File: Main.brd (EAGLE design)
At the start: 125 x 30.3 mm, 41 parts, among them IC1 LM35CZ, Q1 IRLZ44N, T1 2N3904, U1 PIC18F45K22-I/P, X1 22-23-2021

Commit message: Schematic Rearranged
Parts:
- removed C11: (no value), resistor:153CLV-0505
- removed C12: (no value), resistor:C0805
- removed CR1, CR3: AMS1117, AMS1117:SOT223
- removed PSU2: PSU, con-wago-500:W237-102
- removed X1: 22-23-2021, con-molex:22-23-2021
- added C8: 100uF 10v, resistor:E2-5
- added C9: 100nF, resistor:C025-060X050
- added IC2: 7805TV, linear:TO220V
- added IC3: LD117AV33, v-reg:TO220L1
- added PSU1: PSU, con-wago-500:W237-102
- added R2: 0, resistor:0204/7
- C1: value (none) -> 100uF 10v; device resistor:153CLV-0505 -> resistor:E2-5
- C2: value (none) -> 100nF; device resistor:C0805 -> resistor:C025-060X050
- C3, C5: value (none) -> 330uF 16V; device resistor:153CLV-0505 -> resistor:E2-5
- C4, C6: device resistor:C0805 -> resistor:C025-024X044
- C7: value (none) -> 10uF 10v; device resistor:153CLV-0505 -> resistor:E2-5
- LED1, LED3: device led:SML0805 -> led:LED5MM
- R1, R3: value (none) -> 680Ω
- R10, R12, R13, R14, R4, R9: value 4k7 -> 4k7Ω
- R5: value 100 -> 100Ω
- R6, R7, R8: value 10k -> 10kΩ
- moved R12 1110.2 mm to (358.5, 354.1), turned to 90 degrees
- moved R5 1108.7 mm to (368.6, 336.2), turned to 90 degrees
- moved R10 1083.2 mm to (331.8, 347.2), turned to 90 degrees
- moved R9 1056.5 mm to (288.1, 345.4), turned to 90 degrees
- moved R4 1035.6 mm to (256.0, 345.2), turned to 90 degrees
- moved R3 1014.5 mm to (216.9, 345.6), turned to 90 degrees
- moved R1 994.8 mm to (179.9, 345.8), turned to 90 degrees
- moved R13 962.2 mm to (112.3, 348.7), turned to 90 degrees
- moved R14 957.3 mm to (152.1, 325.3), turned to 90 degrees
- moved R8 945.3 mm to (57.5, 349.5), turned to 90 degrees
- moved R7 913.4 mm to (-6.10, 332.3), turned to 90 degrees
- moved LED1 853.0 mm to (-1.27, -825.6), turned to 0 degrees
- moved R6 836.6 mm to (55.9, 266.1), turned to 90 degrees
- moved C2 821.2 mm to (-1.27, -799.5), flipped to the top, turned to 180 degrees
- moved C1 751.6 mm to (-118.9, -731.7), turned to 0 degrees
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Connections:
- net MCU_XI2 renamed MCU_MAIN_OSC2
- net MCU_XO2 renamed MCU_MAIN_OSC1
- net N$19 renamed DOUT_BUZZER
- net N$20 renamed AIN_LM35
- net N$7 renamed DIN_BUTTON_UP
- removed net N$17: R10.1, U$1.3, U1.18
- removed net N$18: R9.1, U$1.4, U1.23
- removed net N$5: R8.2, S4.3, S4.4, U1.36
- removed net N$8: R6.2, S2.3, S2.4, U1.38
- new net +12V: C3.+, C5.+, IC2.1, IC3.3, PSU.1, U$3.30
- new net DIN_BUTTON_DOWN: R8.2, S4.3, S4.4, U1.38
- new net DIN_LOCAL_REMOTE: R6.2, S2.3, S2.4, U1.36
- new net DOUT_HEATER: U1.17
- new net I2C_SCL: R10.2, U$1.3, U1.18
- new net I2C_SDA: R9.2, U$1.4, U1.23
- new net N$2: R2.1, U$3.1
- net +3V3: now also C8.+, C9.1, IC3.2, R2.2; no longer C11.+, C12.1, CR3.2, U$3.1
- net 12V: now also PSU1.1; no longer C3.+, C5.+, CR1.3, CR3.3, PSU.1, PSU2.1, X1.1
- net GND: now also C8.-, C9.2, IC2.2, IC3.1; no longer C11.-, C12.2, CR1.1, CR3.1, PSU2.2
- net N$1: now also LED3.K; no longer LED3.C
- net N$27: no longer U1.17
- net N$29: now also PSU1.2; no longer X1.2
- net N$3: now also LED1.K; no longer LED1.C
- net VCC: now also IC2.3, R10.1, R9.1; no longer CR1.2, R10.2, R9.2
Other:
- board size 125 x 30.3 mm -> 549.4 x 221.8 mm

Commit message: Renamed Resistors and capacitors
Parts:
- removed C1, C8: 100uF 10v, resistor:E2-5
- removed C2, C9: 100nF, resistor:C025-060X050
- removed C3: 330uF 16V, resistor:E2-5
- removed C4, C6: 22pF, resistor:C025-024X044
- removed C7: 10uF 10v, resistor:E2-5
- removed LED3: (no value), led:LED5MM
- removed PSU1: PSU, con-wago-500:W237-102
- removed R12, R4: 4k7Ω, resistor:0204/7
- removed R2: 0, resistor:0204/7
- removed R5: 100Ω, resistor:0204/7
- added C102, C105: 100uF 10v, resistor:E2-5
- added C103, C106: 100nF, resistor:C025-060X050
- added C104: 330uF 16V, resistor:E2-5
- added C107, C108: 22pF, resistor:C025-024X044
- added C109: 10uF 10v, resistor:E2-5
- added CN_HEATER: PSU, con-wago-500:W237-102
- added LED2: (no value), led:LED5MM
- added RX103, RX114: 4k7Ω, resistor:0204/7
- added RX104: 100Ω, resistor:0204/7
- added RX111: 0, resistor:0204/7
- IC2: value 7805TV -> 7805T; device linear:TO220V -> adafruit:TO220H
- moved IC2 949.1 mm to (47.0, 128.6)
- moved LED1 944.9 mm to (200.8, 97.5)
- moved SV1 670.6 mm to (60.4, 91.7)
- moved T1 391.4 mm to (15.7, 58.3), turned to 270 degrees
- moved SG1 369.9 mm to (15.7, 45.6), turned to 270 degrees
- moved IC1 330.7 mm to (15.7, 76.1), turned to 270 degrees
- moved Q3 292.2 mm to (42.1, 47.0), turned to 90 degrees
- moved U$1 130.3 mm to (100.4, 81.0)
- moved U$3 119.7 mm to (99.1, 42.3)
- moved Q1 116.8 mm to (6.81, 86.6), turned to 90 degrees
- moved S4 102.6 mm to (79.5, 89.2)
- moved S3 102.3 mm to (79.4, 80.0)
- moved S2 102.1 mm to (79.3, 70.9)
- moved IC3 90.9 mm to (62.0, 122.3)
- moved U1 80.3 mm to (60.0, 54.6)
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- renumbered C5 to C101, R1 to RX102, R10 to RX106, R13 to RX113, R14 to RX112, R3 to RX101, R6 to RX108, R7 to RX109, R8 to RX110, R9 to RX105
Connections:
- removed net 12V: PSU1.1
- removed net N$27: RX112.2, RX113.2
- net +12V: now also C104.+, CN_HEATER.1; no longer C3.+
- net +3V3: now also C105.+, C106.1, LED2.A, RX111.2; no longer C8.+, C9.1, LED3.A, R2.2
- net DOUT_BUZZER: now also RX114.2; no longer R12.2
- net DOUT_HEATER: now also RX112.2, RX113.2
- net GND: now also C102.-, C103.2, C104.-, C105.-, C106.2, C107.2, C108.2, C109.-; no longer C1.-, C2.2, C3.-, C4.2, C6.2, C7.-, C8.-, C9.2
- net MCLR: now also C109.+, RX103.1, RX104.2; no longer C7.+, R4.1, R5.2
- net MCU_MAIN_OSC1: now also C108.1; no longer C6.1
- net MCU_MAIN_OSC2: now also C107.1; no longer C4.1
- net N$1: now also LED2.K; no longer LED3.K
- net N$2: now also RX111.1; no longer R2.1
- net N$25: now also RX114.1; no longer R12.1
- net N$29: now also CN_HEATER.2; no longer PSU1.2
- net N$6: now also RX104.1; no longer R5.1
- net VCC: now also C102.+, C103.1, RX103.2; no longer C1.+, C2.1, R4.2

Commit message: Components placed, Previous to start routing
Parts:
- removed C101, C104: 330uF 16V, resistor:E2-5
- removed C102, C105: 100uF 10v, resistor:E2-5
- removed C103, C106: 100nF, resistor:C025-060X050
- removed C107, C108: 22pF, resistor:C025-024X044
- removed C109: 10uF 10v, resistor:E2-5
- removed RX101, RX102: 680Ω, resistor:0204/7
- removed RX103, RX105, RX106, RX112, RX113, RX114: 4k7Ω, resistor:0204/7
- removed RX104: 100Ω, resistor:0204/7
- removed RX108, RX109, RX110: 10kΩ, resistor:0204/7
- removed RX111: 0, resistor:0204/7
- added C1, C4: 330uF 16V, resistor:E2-5
- added C2, C5: 100uF 10v, resistor:E2-5
- added C3, C6: 100nF, resistor:C025-060X050
- added C7, C8: 22pF, resistor:C025-024X044
- added C9: 10uF 10v, resistor:E2-5
- added R1, R2: 680Ω, resistor:0204/7
- added R10, R8, R9: 10kΩ, resistor:0204/7
- added R11: 0, resistor:0204/7
- added R12, R13, R14, R3, R5, R6: 4k7Ω, resistor:0204/7
- added R4: 100Ω, resistor:0204/7
- IC1: value LM35CZ -> 7805T; device lm35:TO92 -> adafruit:TO220H
- IC2: value 7805T -> LD117AV33; device adafruit:TO220H -> v-reg:TO220L1
- IC3: value LD117AV33 -> LM35CZ; device v-reg:TO220L1 -> lm35:TO92
- moved LED1 174.7 mm to (27.8, 72.7), turned to 180 degrees
- moved LED2 153.1 mm to (48.1, 72.7), turned to 180 degrees
- moved IC3 102.8 mm to (5.31, 36.5), turned to 270 degrees
- moved S4 80.6 mm to (25.9, 29.0), turned to 180 degrees
- moved S3 80.1 mm to (26.0, 20.3), turned to 180 degrees
- moved SV1 61.7 mm to (4.04, 66.4), turned to 270 degrees
- moved S2 61.7 mm to (26.1, 39.6), turned to 180 degrees
- moved IC2 42.3 mm to (51.8, 86.6)
- moved S1 40.9 mm to (26.1, 51.1)
- moved Q3 38.6 mm to (26.6, 11.7), turned to 180 degrees
- moved T1 38.5 mm to (5.31, 21.2)
- moved PSU 38.1 mm to (9.88, 96.0)
- moved CN_HEATER 38.1 mm to (9.93, 81.3)
- moved SG1 35.1 mm to (10.0, 10.9), turned to 180 degrees
- moved Q1 34.9 mm to (4.27, 51.8)
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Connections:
- net +12V: now also C1.+, C4.+, IC1.1, IC2.3; no longer C101.+, C104.+, IC2.1, IC3.3
- net +3V3: now also C5.+, C6.1, IC2.2, R11.2; no longer C105.+, C106.1, IC3.2, RX111.2
- net AIN_LM35: now also IC3.2; no longer IC1.2
- net DIN_BUTTON_DOWN: now also R10.2; no longer RX110.2
- net DIN_BUTTON_UP: now also R9.2; no longer RX109.2
- net DIN_LOCAL_REMOTE: now also R8.2; no longer RX108.2
- net DOUT_BUZZER: now also R14.2; no longer RX114.2
- net DOUT_HEATER: now also R12.2, R13.2; no longer RX112.2, RX113.2
- net GND: now also C1.-, C2.-, C3.2, C4.-, C5.-, C6.2, C7.2, C8.2, C9.-, IC1.2, IC2.1, IC3.3, R1.1, R10.1, R13.1, R2.1, R8.1, R9.1; no longer C101.-, C102.-, C103.2, C104.-, C105.-, C106.2, C107.2, C108.2, C109.-, IC1.3, IC2.2, IC3.1, RX101.1, RX102.1, RX108.1, RX109.1, RX110.1, RX113.1
- net I2C_SCL: now also R6.2; no longer RX106.2
- net I2C_SDA: now also R5.2; no longer RX105.2
- net MCLR: now also C9.+, R3.1, R4.2; no longer C109.+, RX103.1, RX104.2
- net MCU_MAIN_OSC1: now also C8.1; no longer C108.1
- net MCU_MAIN_OSC2: now also C7.1; no longer C107.1
- net N$1: now also R2.2; no longer RX102.2
- net N$2: now also R11.1; no longer RX111.1
- net N$25: now also R14.1; no longer RX114.1
- net N$28: now also R12.1; no longer RX112.1
- net N$3: now also R1.2; no longer RX101.2
- net N$6: now also R4.1; no longer RX104.1
- net VCC: now also C2.+, C3.1, IC1.3, IC3.1, R3.2, R5.1, R6.1; no longer C102.+, C103.1, IC1.1, IC2.3, RX103.2, RX105.1, RX106.1
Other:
- board size 549.4 x 221.8 mm -> 91.2 x 105.5 mm

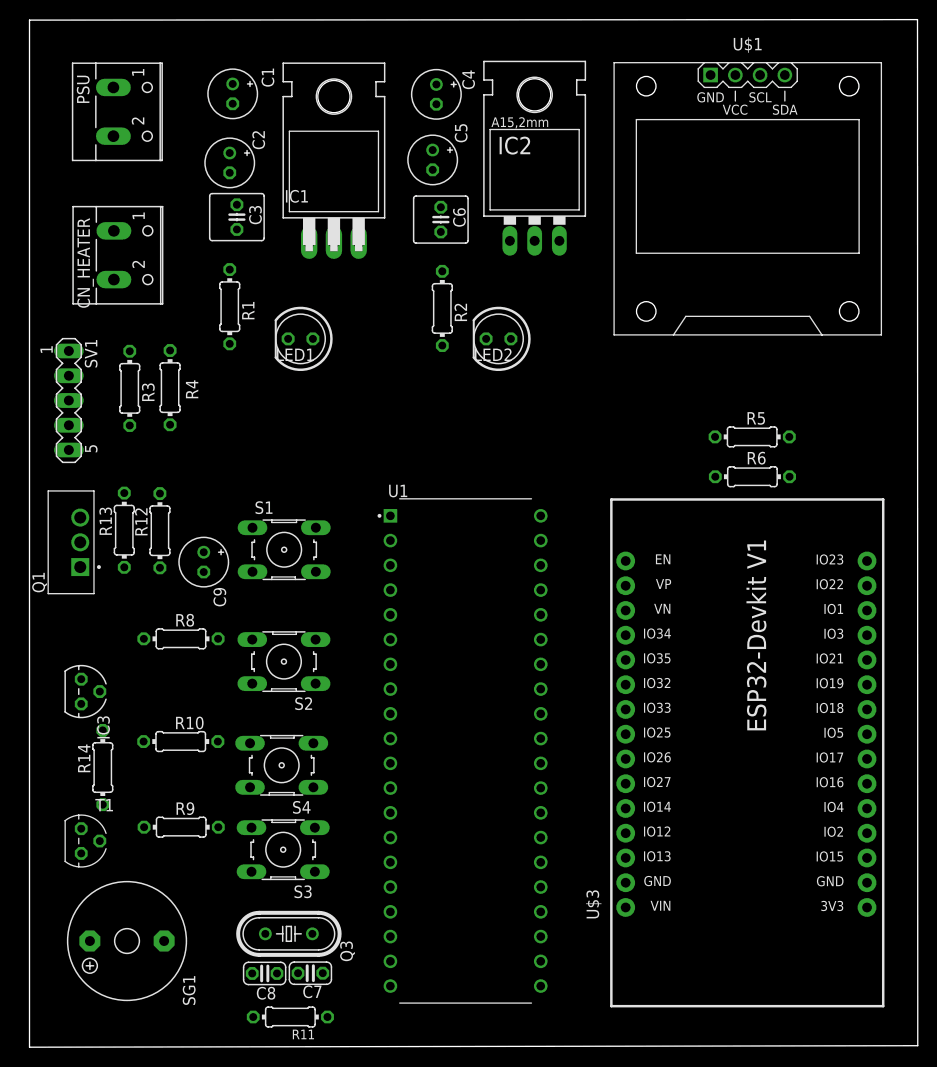
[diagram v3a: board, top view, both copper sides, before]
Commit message: Routing. I2C lines Pending
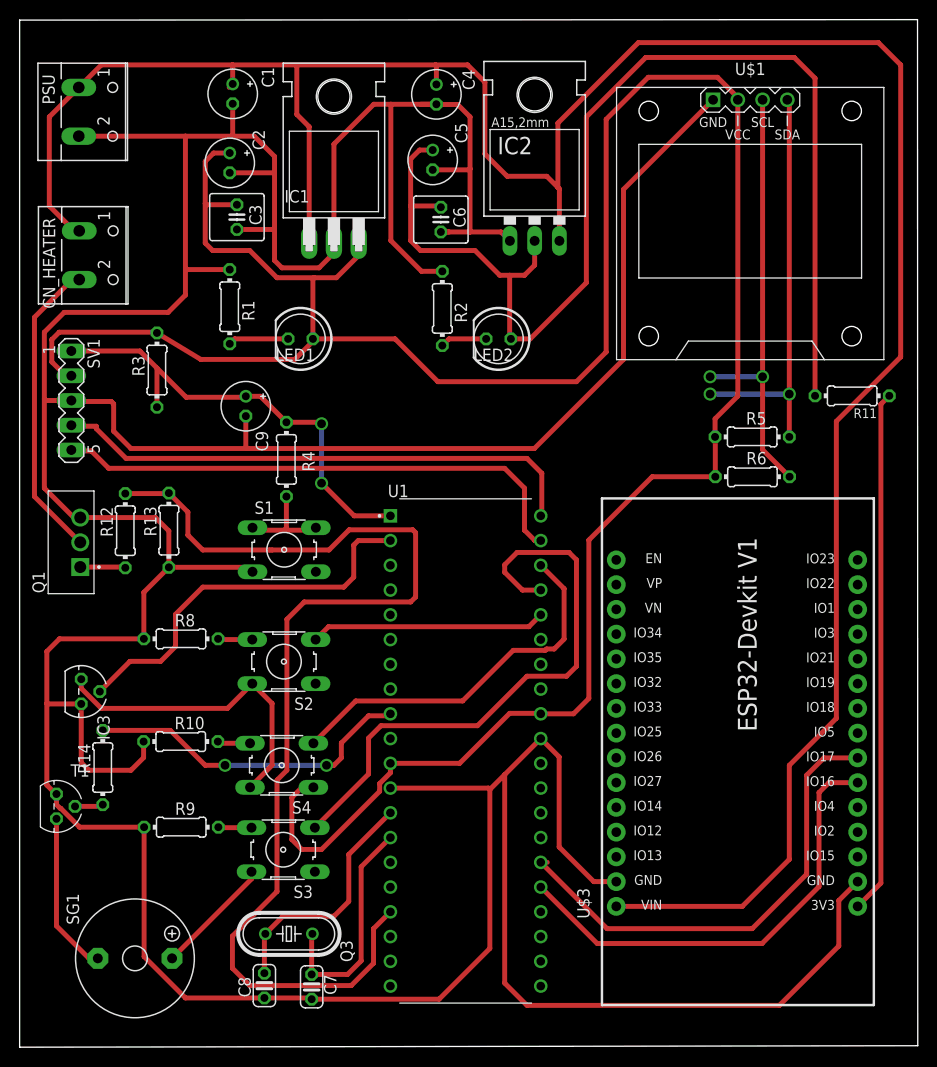
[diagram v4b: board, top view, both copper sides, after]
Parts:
- moved R11 86.0 mm to (84.4, 66.9)
- moved C9 16.6 mm to (22.2, 65.8)
- moved R4 14.0 mm to (26.4, 60.4)
- moved R13 4.57 mm to (14.3, 53.1)
- moved T1 4.37 mm to (2.77, 24.7)
- moved CN_HEATER 3.56 mm to (6.38, 81.3)
- moved PSU 3.56 mm to (6.32, 96.0)
- moved R12 3.56 mm to (9.83, 53.0)
- moved R3 3.37 mm to (13.1, 69.5), turned to 90 degrees
- moved U$1 2.55 mm to (74.0, 84.6)
- moved SG1 1.95 mm to (10.8, 9.14), turned to 0 degrees
- moved C7 1.40 mm to (29.0, 6.22), turned to 270 degrees
- moved C8 1.24 mm to (24.1, 6.35), turned to 270 degrees
- moved U$3 0.97 mm to (71.5, 37.3)
- moved SV1 0.25 mm to (4.29, 66.4)
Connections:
- net GND: now also U$3.29; no longer U$3.28
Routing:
- net GND: track 0.00 -> 541.4 mm
- net VCC: track 0.00 -> 310.3 mm
- net +12V: track 0.00 -> 259.3 mm
- net +3V3: track 0.00 -> 124.5 mm
- net DOUT_HEATER: track 0.00 -> 115.6 mm
- net DIN_BUTTON_UP: track 0.00 -> 63.6 mm
- net PGD: track 0.00 -> 54.9 mm
- net PGC: track 0.00 -> 54.6 mm
- net N$2: track 0.00 -> 53.7 mm
- net RX1-TX2: track 0.00 -> 49.2 mm
- net MCLR: track 0.00 -> 47.4 mm, vias 0 -> 2
- net TX1-RX2: track 0.00 -> 47.4 mm
- net I2C_SCL: track 0.00 -> 45.2 mm, vias 0 -> 2
- net I2C_SDA: track 0.00 -> 42.8 mm, vias 0 -> 2
- net DIN_BUTTON_DOWN: track 0.00 -> 42.1 mm
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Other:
- board size 91.2 x 105.5 mm -> 92.2 x 105.5 mm

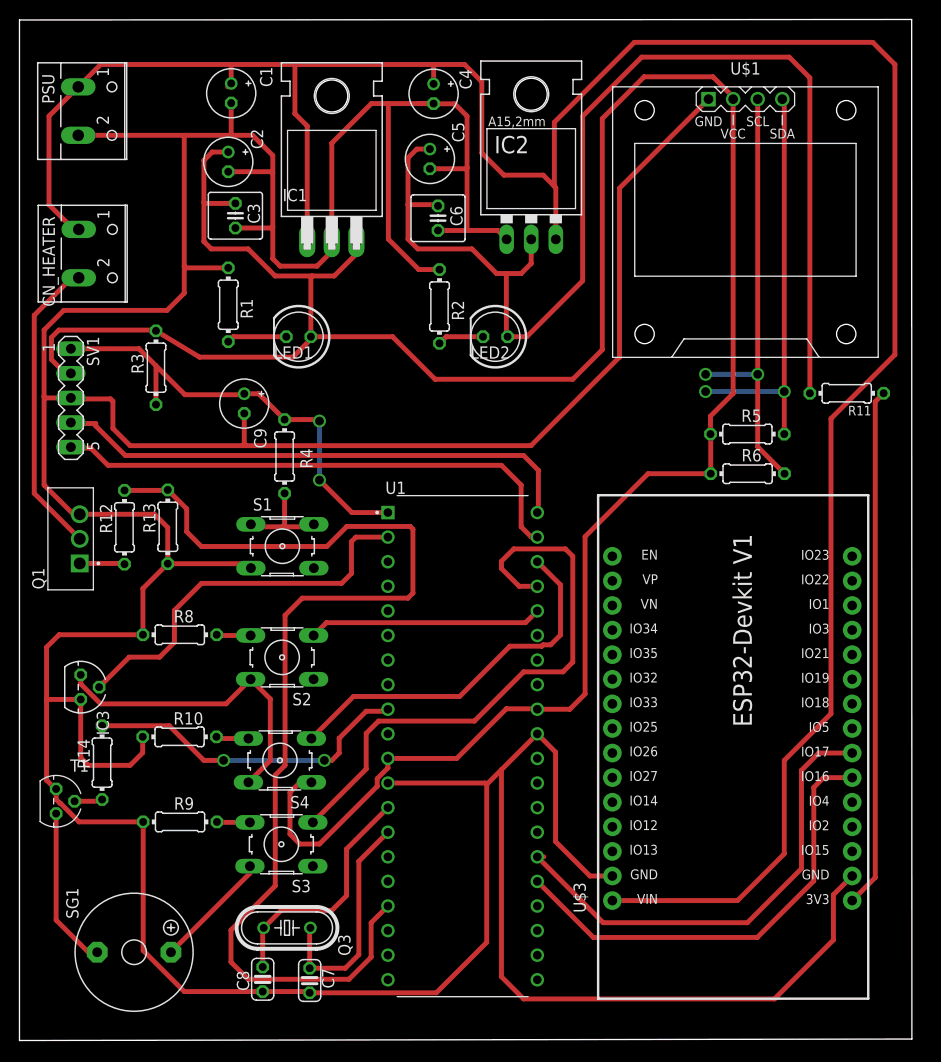
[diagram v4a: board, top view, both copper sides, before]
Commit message: Routing complete, Pending swap routes from top to botton
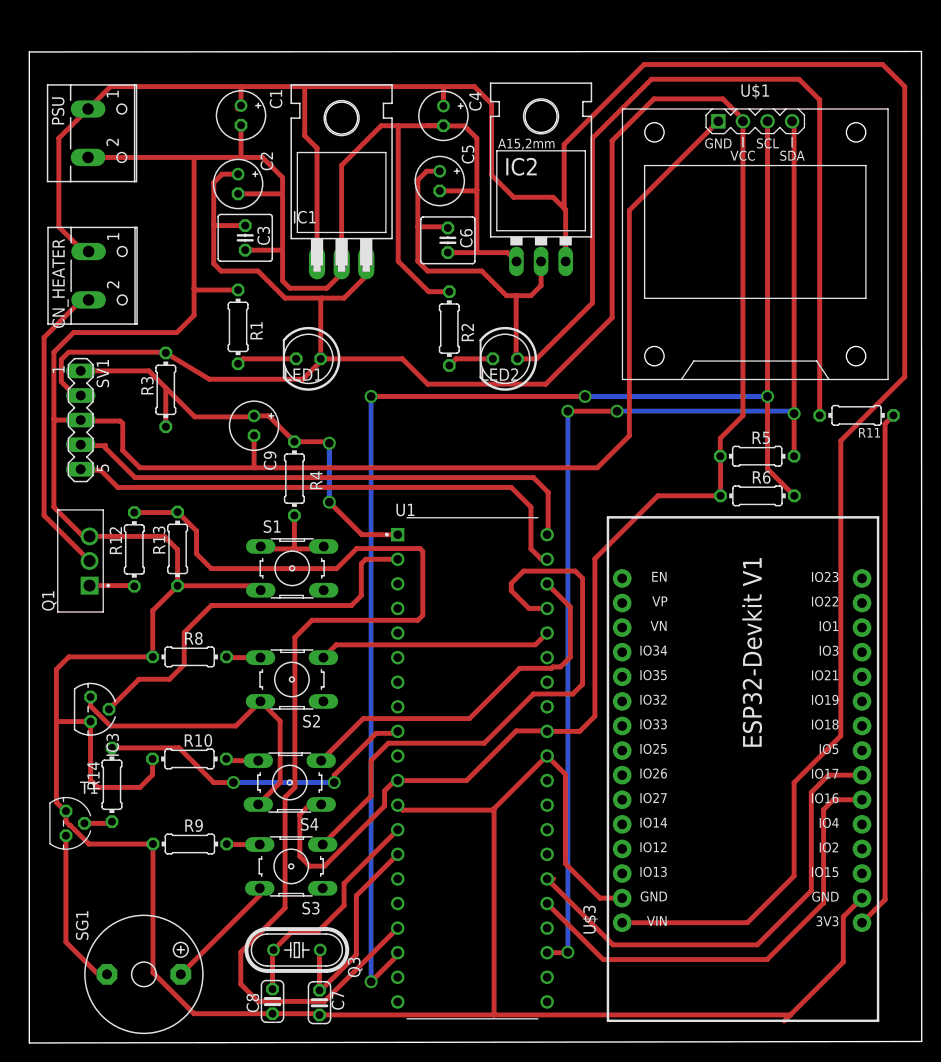
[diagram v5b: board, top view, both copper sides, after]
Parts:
- moved C9 2.50 mm to (23.2, 63.5)
- moved C4 2.50 mm to (42.8, 95.5)
- moved R11 2.50 mm to (85.4, 64.6)
- moved R6 2.50 mm to (75.2, 56.3)
- moved U$1 2.50 mm to (75.0, 82.3)
- moved U$3 2.50 mm to (72.5, 35.1)
- moved C3 2.50 mm to (22.3, 82.9)
- moved IC1 2.50 mm to (32.3, 90.5)
- moved LED1 2.50 mm to (28.8, 70.4)
- moved R9 2.50 mm to (16.6, 20.3)
- moved CN_HEATER 2.50 mm to (7.39, 79.0)
- moved IC3 2.50 mm to (6.32, 34.2)
- moved PSU 2.50 mm to (7.34, 93.7)
- moved Q1 2.50 mm to (5.28, 49.6)
- moved R10 2.50 mm to (16.5, 29.1)
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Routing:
- net I2C_SCL: track 45.2 -> 145.4 mm, vias 2 -> 4
- net I2C_SDA: track 42.8 -> 116.2 mm, vias 2 -> 4
- net GND: track 541.4 -> 527.8 mm
- net VCC: track 310.3 -> 305.4 mm
- net MCU_MAIN_OSC2: track 23.7 -> 21.7 mm
- net DOUT_HEATER: track 115.6 -> 113.6 mm
- net MCU_MAIN_OSC1: track 24.9 -> 23.4 mm
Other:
- board size 92.2 x 105.5 mm -> 92.2 x 102.4 mm
